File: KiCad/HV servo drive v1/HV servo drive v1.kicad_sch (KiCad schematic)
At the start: 0 parts

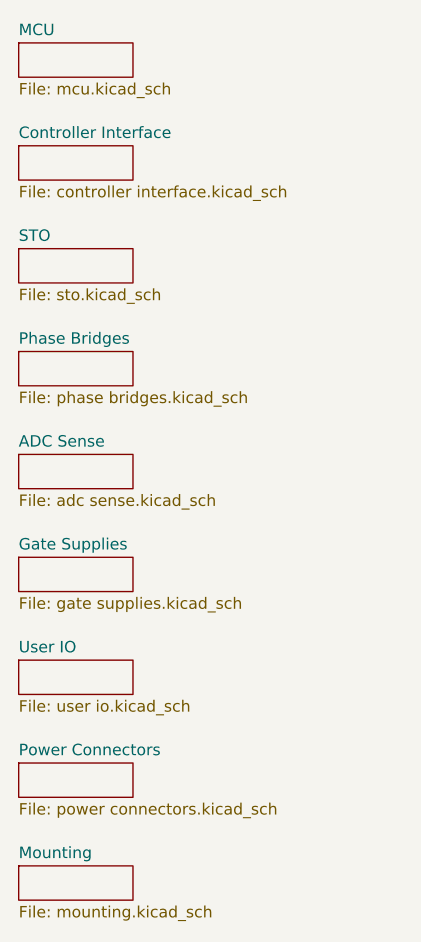
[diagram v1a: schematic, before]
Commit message: start rev 2 changes
fix component references, fix rj45 and dc-dc converter footprints, add RLC filters on all power connectors, add more mounting holes
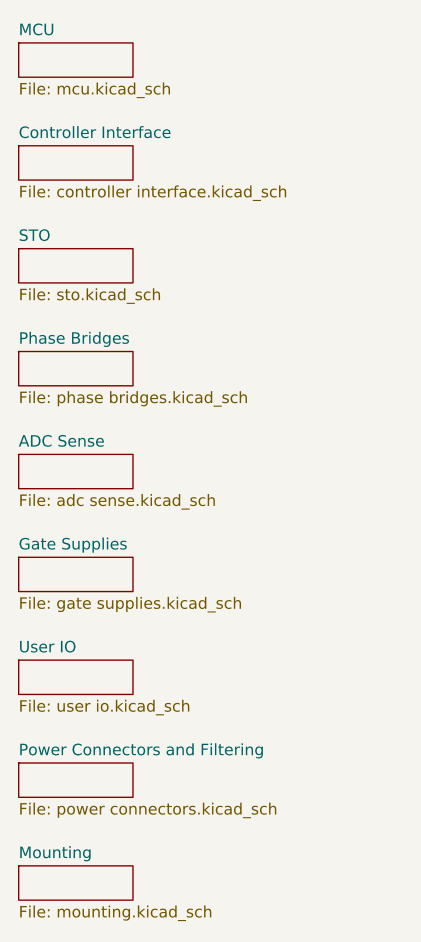
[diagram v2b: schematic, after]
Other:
- sheet Power Connectors renamed Power Connectors and Filtering
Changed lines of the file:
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@@
 			(color 0 0 0 0.0000)
 		)
-		(property "Sheetname" "Power Connectors"
+		(property "Sheetname" "Power Connectors and Filtering"
 			(at 30.48 127.5584 0)
 			(effects
